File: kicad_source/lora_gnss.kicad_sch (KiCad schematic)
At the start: 32 parts, among them Q1 NTR4171P, SW3 SW_SPDT, U2 Ai-Thinker-Ra-01, U3 NEO-M8N, U5 24LC32, U6 BME280, U7 TPS3839DBZ, U8 TPS73630DBV, U9 MCP73832-2-OT

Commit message: glued project together
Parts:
- removed BT1: Battery_Cell, generationmake:KEYSTONE_1043, symbol Device:Battery_Cell
- removed C21, C22, C23: 2.2 uF, Capacitor_SMD:C_0603_1608Metric, symbol Device:C_Small
- removed D3: LED_Small, LED_SMD:LED_0603_1608Metric, symbol Device:LED_Small
- removed D4: MBR120, Diode_SMD:D_SOD-123, symbol Device:D_Schottky_Small
- removed F1: SF-1206S050, Fuse:Fuse_1206_3216Metric, symbol Device:Fuse
- removed Q1: NTR4171P, Package_TO_SOT_SMD:SOT-23, symbol Device:Q_PMOS_GSD
- removed R14, R16: 4k7, Resistor_SMD:R_0603_1608Metric, symbol Device:R_Small
- removed R15: 2k, Resistor_SMD:R_0603_1608Metric, symbol Device:R_Small
- removed SW3: SW_SPDT, Button_Switch_THT:SW_Slide-03_Wuerth-WS-SLTV_10x2.5x6.4_P2.54mm, symbol Switch:SW_SPDT_312
- removed U7: TPS3839DBZ, Package_TO_SOT_SMD:SOT-23, symbol Power_Supervisor:TPS3839DBZ
- removed U8: TPS73630DBV, Package_TO_SOT_SMD:SOT-23-5, symbol Regulator_Linear:TPS73630DBV
- removed U9: MCP73832-2-OT, Package_TO_SOT_SMD:SOT-23-5, symbol Battery_Management:MCP73832-2-OT
- added J1: BM04B-SRSS-TB, Connector_JST:JST_SH_BM04B-SRSS-TB_1x04-1MP_P1.00mm_Vertical, symbol Connector_Generic_MountingPin:Conn_01x04_MountingPin
- added R12, R4: 10k, Resistor_SMD:R_0603_1608Metric, symbol Device:R_Small
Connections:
- net +3V3: now also J1.2 (Pin_2), R12.1, R4.1
- net GND: now also J1.1 (Pin_1)
- net I2C_SCL: now also J1.4 (Pin_4), R12.2
- net I2C_SDA: now also J1.3 (Pin_3), R4.2
- no-connect marks 14 -> 12
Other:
- note added: "quiic connector"
- note removed: "charging current set to 500 mA (R15 = 2k)"
- title: RP2040LoRaTracker -> LoRaZeroHAT

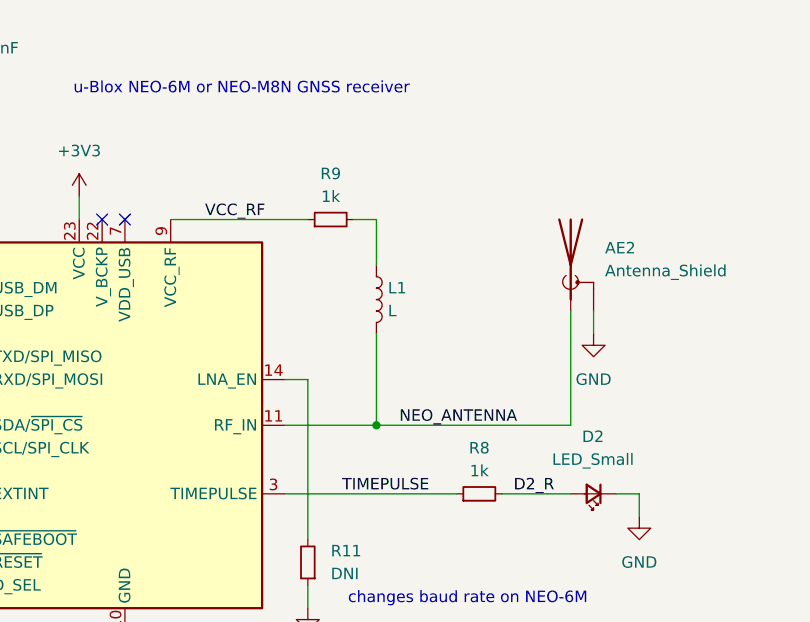
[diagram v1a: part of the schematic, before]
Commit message: connected schematic to layout
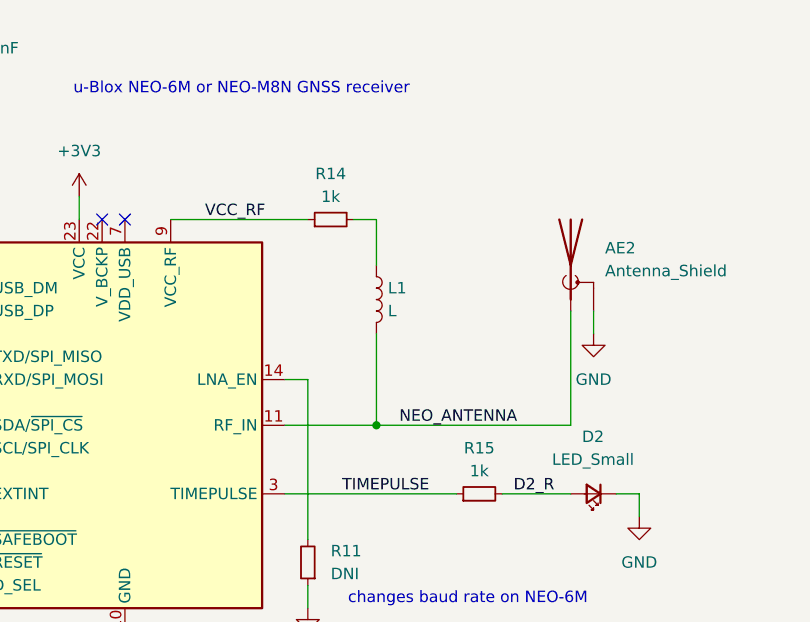
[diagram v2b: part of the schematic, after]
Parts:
- renumbered R9 to R14, R8 to R15
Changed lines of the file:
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@@
 		(dnp no)
 		(fields_autoplaced yes)
-		(property "Reference" "R8"
+		(property "Reference" "R15"
 			(at 127 76.2 90)
 			(effects
@@
 			(project "RP2040LoRaTracker"
 				(path "/143f7a5b-9016-4d2c-b741-f535648590f8/eaeb2dbb-82d1-4bb1-aa6e-4edb004b54b5"
-					(reference "R8")
+					(reference "R15")
 					(unit 1)
 				)
@@
 		(dnp no)
 		(fields_autoplaced yes)
-		(property "Reference" "R9"
+		(property "Reference" "R14"
 			(at 110.49 45.72 90)
 			(effects
@@
 			(project "RP2040LoRaTracker"
 				(path "/143f7a5b-9016-4d2c-b741-f535648590f8/eaeb2dbb-82d1-4bb1-aa6e-4edb004b54b5"
-					(reference "R9")
-					(unit 1)
-				)
+					(reference "R14")
+					(unit 1)
+				)

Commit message: made first connections
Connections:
- net +3V3 renamed +3.3V

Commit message: updated layout
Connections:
- net LORA_DIO0 renamed LORA_INT
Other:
- note added: "DIO0 is configured as interrupt"
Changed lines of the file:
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@@
+		)
+	)
+	(text "DIO0 is configured as interrupt"
+		(exclude_from_sim no)
+		(at 251.714 76.2 0)
+		(effects
+			(font
+				(size 1.27 1.27)
+			)
 		)
 	)
@@
 		)
 	)
-	(label "LORA_DIO0"
+	(label "LORA_INT"
 		(at 220.98 71.12 0)
 		(effects
@@
 		)
 	)
-	(global_label "LORA_DIO0"
+	(global_label "LORA_INT"
 		(shape output)
 		(at 234.95 71.12 0)
@@
 		)
 		(property "Intersheetrefs" "${INTERSHEET_REFS}"
-			(at 248.0348 71.12 0)
+			(at 246.5229 71.12 0)
 			(effects
 				(font

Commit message: schaltplan neu annotiert
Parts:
- renumbered AE2 to AE1, AE1 to AE2, C16 to C1, C17 to C2, C20 to C3, C18 to C4, C19 to C5, D2 to D1, L1 to L4, R10 to R12, R11 to R13, R4 to R15, R15 to R16, R12 to R17, U5 to U1, U3 to U2, U2 to U3, U6 to U4

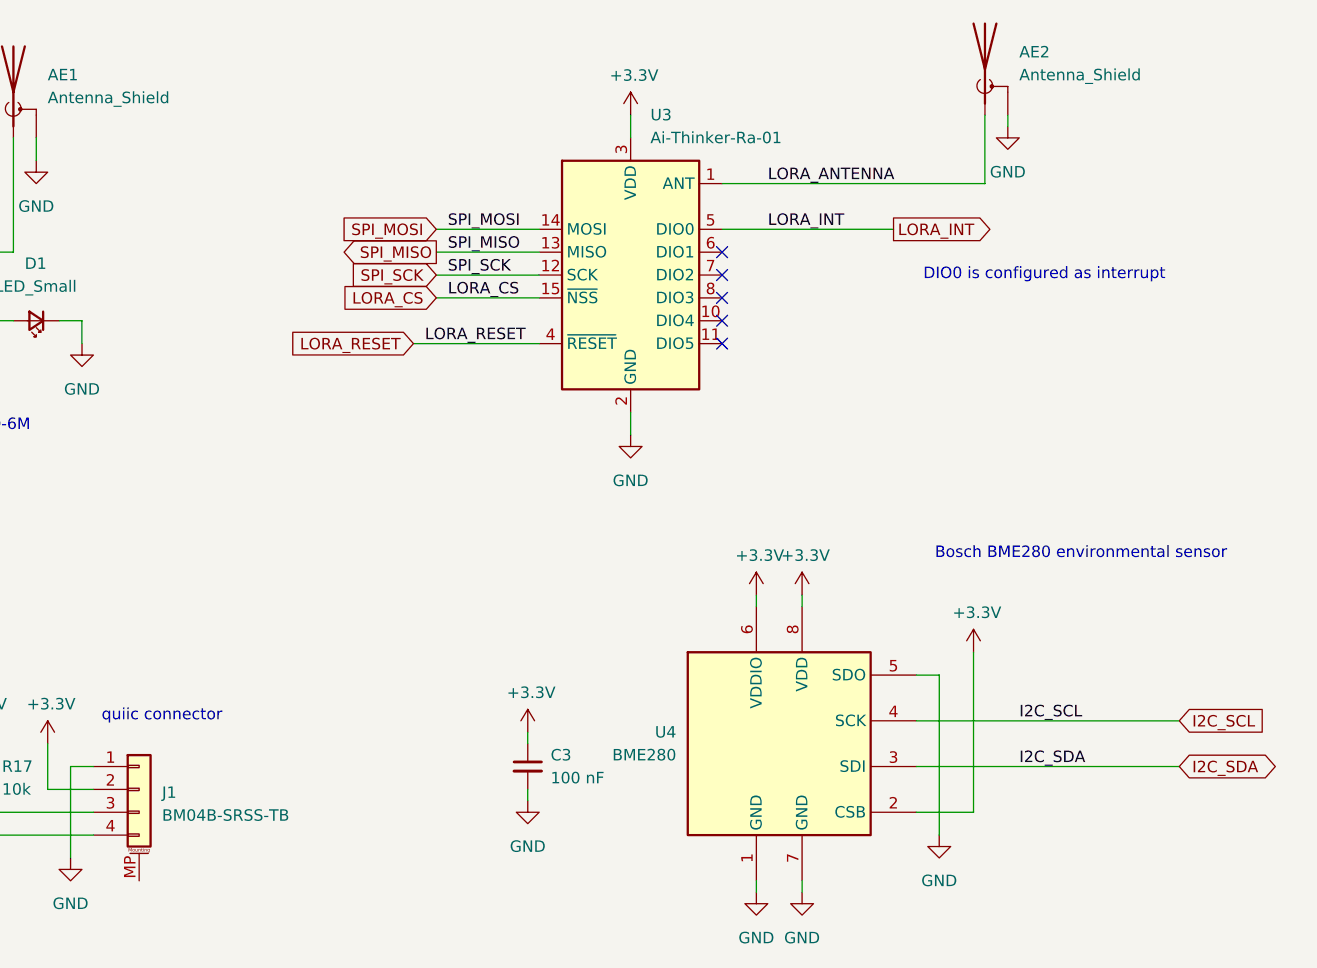
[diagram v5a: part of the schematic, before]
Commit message: updated layout
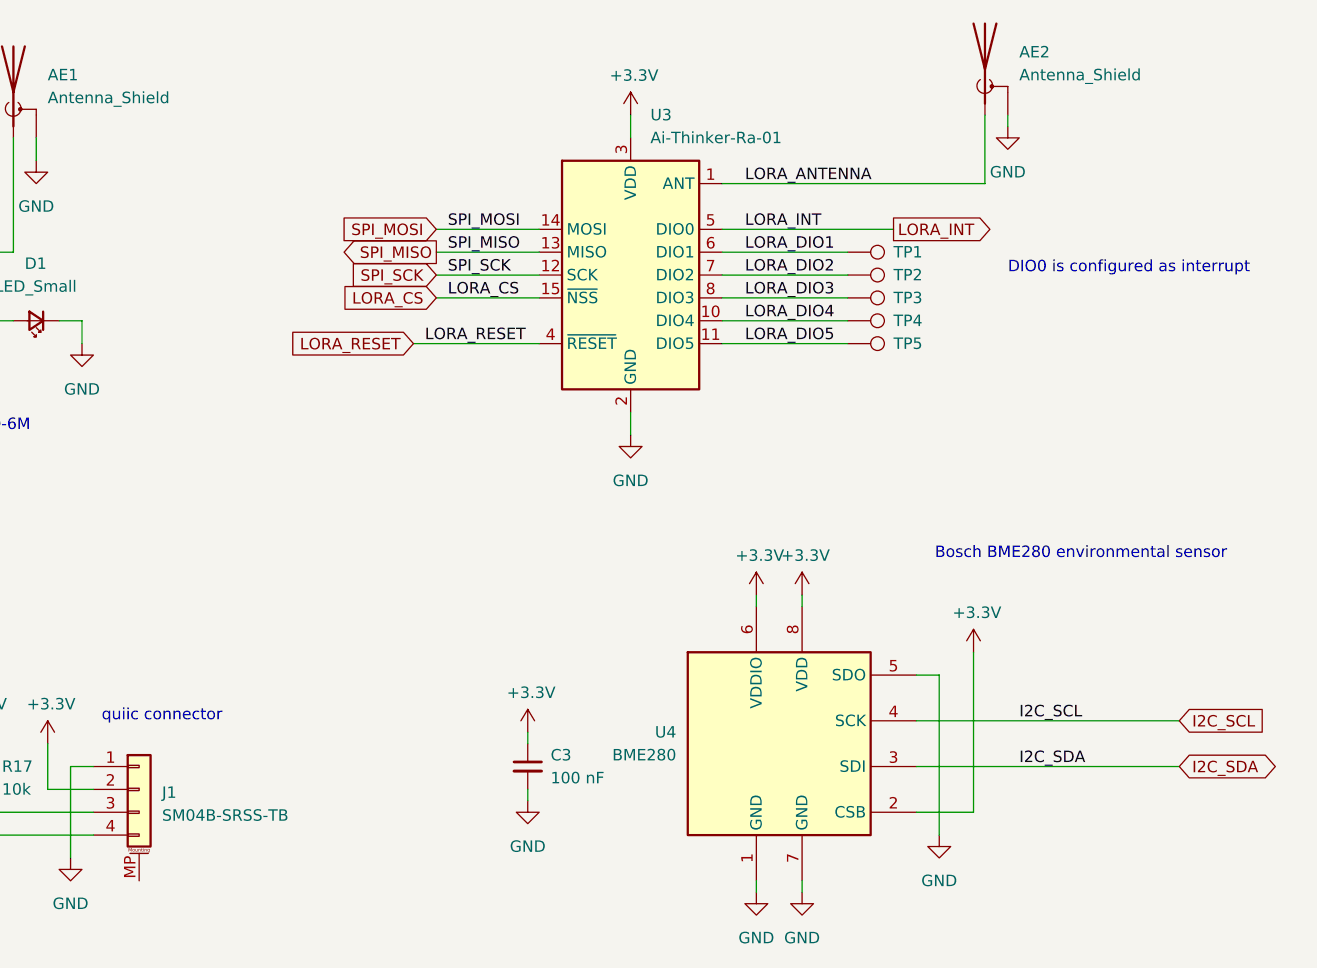
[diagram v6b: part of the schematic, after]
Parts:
- added TP1, TP2, TP3, TP4, TP5: TestPoint, TestPoint:TestPoint_Pad_D1.0mm, symbol Connector:TestPoint
- J1: value BM04B-SRSS-TB -> SM04B-SRSS-TB; footprint Connector_JST:JST_SH_BM04B-SRSS-TB_1x04-1MP_P1.00mm_Vertical -> Connector_JST:JST_SH_SM04B-SRSS-TB_1x04-1MP_P1.00mm_Horizontal
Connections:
- net LORA_DIO4: now reaches U3.10 (DIO4)
- net LORA_DIO4: now also TP4.1
- net LORA_DIO5: now reaches U3.11 (DIO5)
- net LORA_DIO5: now also TP5.1
- net LORA_DIO1: now reaches U3.6 (DIO1)
- net LORA_DIO1: now also TP1.1
- net LORA_DIO2: now reaches U3.7 (DIO2)
- net LORA_DIO2: now also TP2.1
- net LORA_DIO3: now reaches U3.8 (DIO3)
- net LORA_DIO3: now also TP3.1
- no-connect marks 12 -> 7

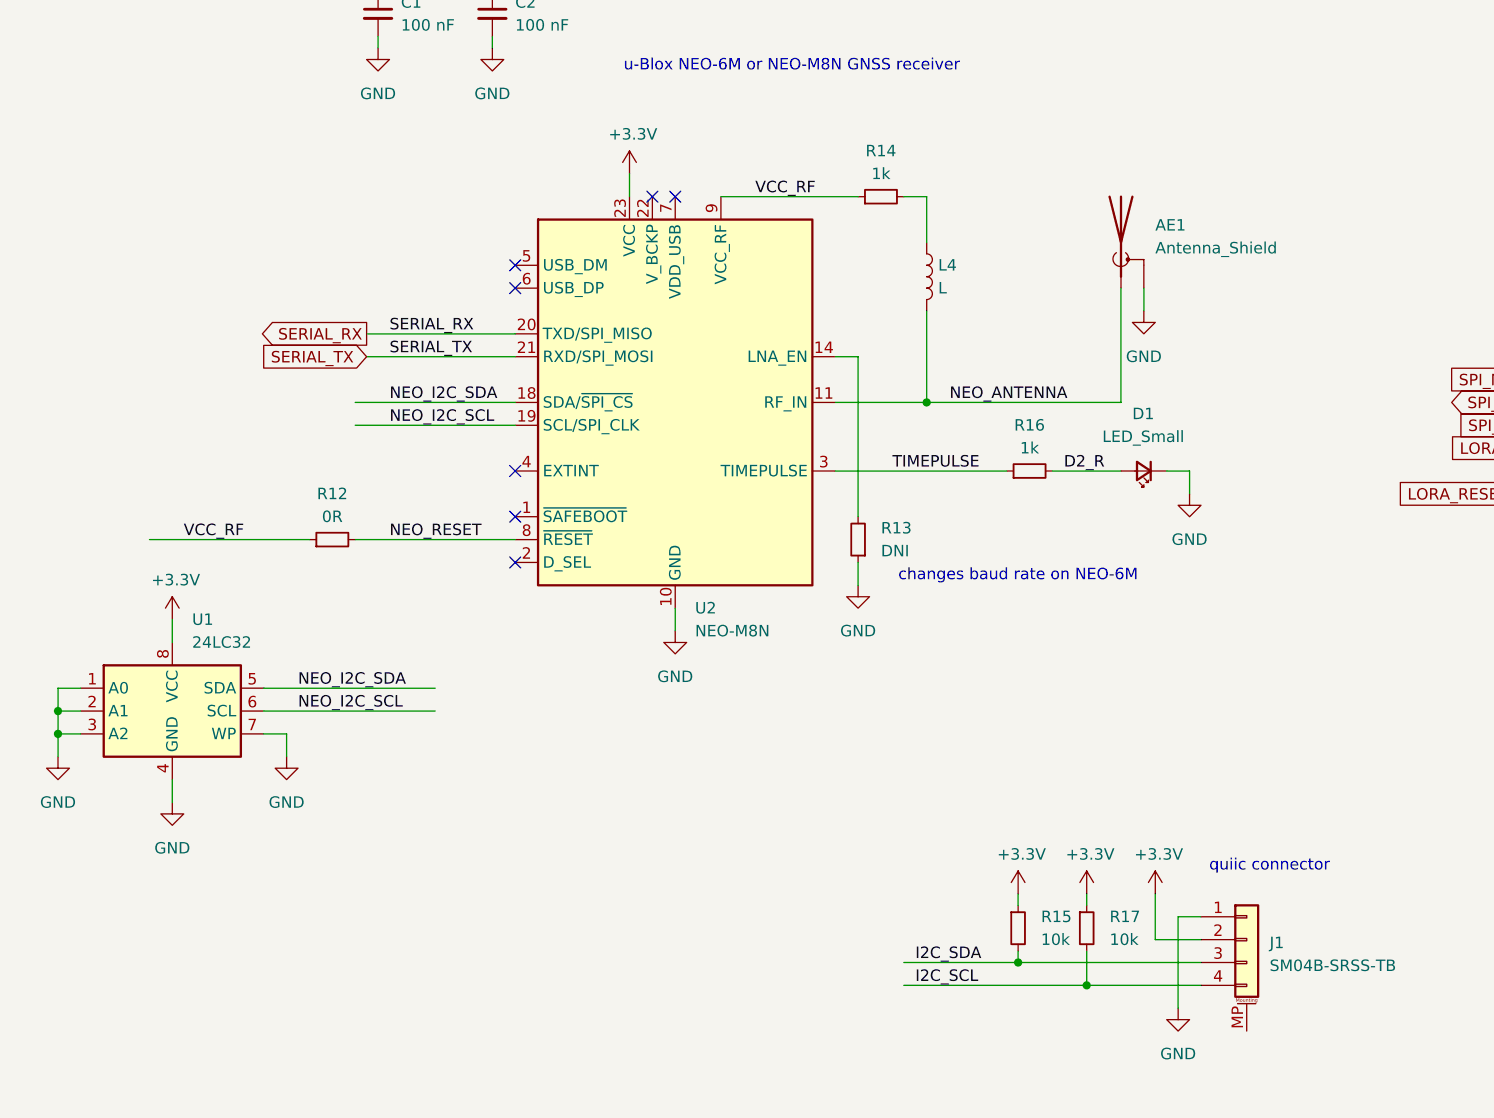
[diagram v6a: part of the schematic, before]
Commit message: added capacitor C6 on u-blox VCC_RF
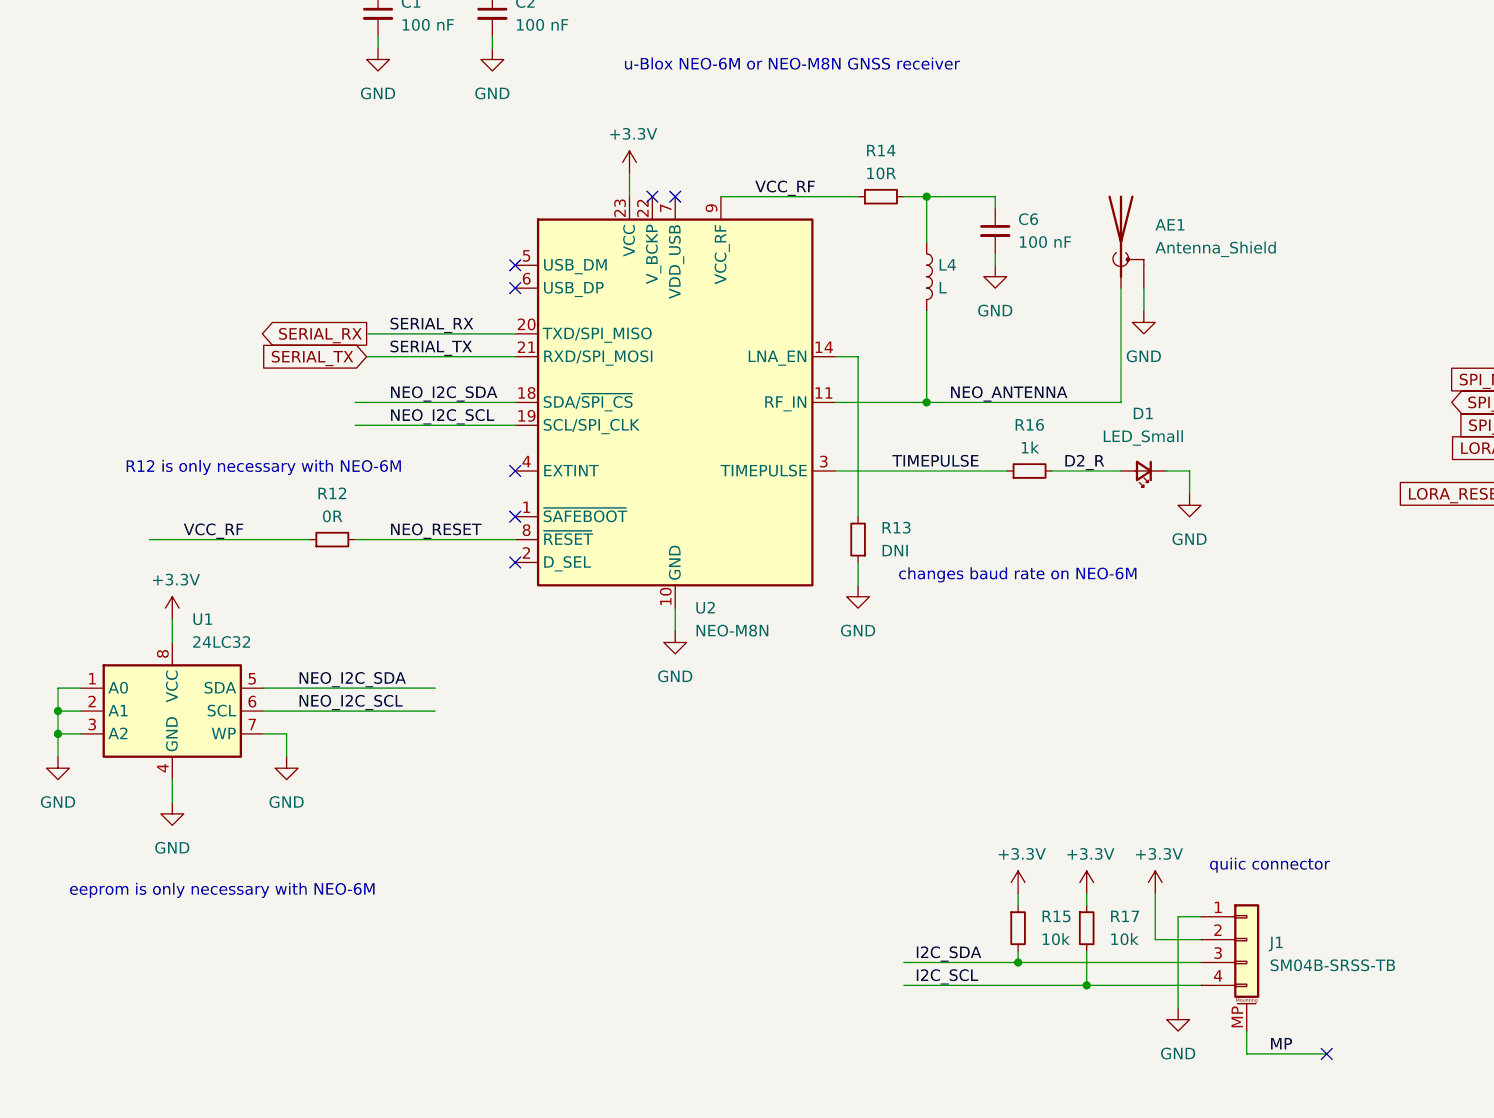
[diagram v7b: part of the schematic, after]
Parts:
- added C6: 100 nF, Capacitor_SMD:C_0603_1608Metric, symbol Device:C_Small
- R14: value 1k -> 10R
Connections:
- net GND: now also C6.2
- net at L4.1, R14.2: now also C6.1
- net MP: now reaches J1.MP (MountPin)
- no-connect marks 7 -> 8
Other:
- note added: "R12 is only necessary with NEO-6M"
- note added: "eeprom is only necessary with NEO-6M"
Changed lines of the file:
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@@
 	)
 	(junction
+		(at 115.57 50.8)
+		(diameter 0)
+		(color 0 0 0 0)
+	)
+	(junction
 		(at 125.73 135.89)
 		(diameter 0)
@@
 	)
 	(no_connect
+		(at 160.02 146.05)
+	)
+	(no_connect
 		(at 69.85 81.28)
 	)
@@
 	(wire
 		(pts
+			(xy 151.13 146.05) (xy 151.13 143.51)
+		)
+		(stroke
+			(width 0)
+			(type default)
+		)
+	)
+	(wire
+		(pts
+			(xy 115.57 50.8) (xy 123.19 50.8)
+		)
+		(stroke
+			(width 0)
+			(type default)
+		)
+	)
+	(wire
+		(pts
 			(xy 54.61 26.67) (xy 54.61 27.94)
 		)
@@
 	(wire
 		(pts
+			(xy 160.02 146.05) (xy 151.13 146.05)
+		)
+		(stroke
+			(width 0)
+			(type default)
+		)
+	)
+	(wire
+		(pts
 			(xy 219.71 111.76) (xy 219.71 113.03)
 		)
@@
 	(wire
 		(pts
+			(xy 123.19 50.8) (xy 123.19 52.07)
+		)
+		(stroke
+			(width 0)
+			(type default)
+		)
+	)
+	(wire
+		(pts
 			(xy 125.73 135.89) (xy 146.05 135.89)
 		)
@@
 	(wire
 		(pts
+			(xy 123.19 57.15) (xy 123.19 58.42)
+		)
+		(stroke
+			(width 0)
+			(type default)
+		)
+	)
+	(wire
+		(pts
 			(xy 195.58 31.75) (xy 195.58 33.02)
 		)
@@
 		)
 	)
+	(text "R12 is only necessary with NEO-6M"
+		(exclude_from_sim no)
+		(at 41.91 81.026 0)
+		(effects
+			(font
+				(size 1.27 1.27)
+			)
+		)
+	)
+	(text "eeprom is only necessary with NEO-6M"
+		(exclude_from_sim no)
+		(at 37.338 128.016 0)
+		(effects
+			(font
+				(size 1.27 1.27)
+			)
+		)
+	)
 	(text "changes baud rate on NEO-6M"
 		(exclude_from_sim no)
@@
 		)
 	)
+	(label "MP"
+		(at 153.67 146.05 0)
+		(effects
+			(font
+				(size 1.27 1.27)
+			)
+			(justify left bottom)
+		)
+	)
 	(label "TIMEPULSE"
 		(at 111.76 81.28 0)
@@
 	)
 	(symbol
+		(lib_id "power:GND")
+		(at 123.19 58.42 0)
+		(unit 1)
+		(exclude_from_sim no)
+		(in_bom yes)
+		(on_board yes)
+		(dnp no)
+		(fields_autoplaced yes)
+		(property "Reference" "#PWR40"
+			(at 123.19 64.77 0)
+			(effects
+				(font
+					(size 1.27 1.27)
+				)
+				(hide yes)
+			)
+		)
+		(property "Value" "GND"
+			(at 123.19 63.5 0)
+			(effects
+				(font
+					(size 1.27 1.27)
+				)
+			)
+		)
+		(property "Footprint" ""
+			(at 123.19 58.42 0)
+			(effects
+				(font
+					(size 1.27 1.27)
+				)
+				(hide yes)
+			)
+		)
+		(property "Datasheet" ""
+			(at 123.19 58.42 0)
+			(effects
+				(font
+					(size 1.27 1.27)
+				)
+				(hide yes)
+			)
+		)
+		(property "Description" "Power symbol creates a global label with name \"GND\" , ground"
+			(at 123.19 58.42 0)
+			(effects
+				(font
+					(size 1.27 1.27)
+				)
+				(hide yes)
+			)
+		)
+		(pin "1"
+		)
+		(instances
+			(project "LoRaZeroHAT"
+				(path "/143f7a5b-9016-4d2c-b741-f535648590f8/eaeb2dbb-82d1-4bb1-aa6e-4edb004b54b5"
+					(reference "#PWR40")
+					(unit 1)
+				)
+			)
+		)
+	)
+	(symbol
 		(lib_id "Device:R_Small")
 		(at 107.95 88.9 180)
@@
 			)
 		)
-		(property "Value" "1k"
+		(property "Value" "10R"
 			(at 110.49 48.26 90)
 			(effects
@@
 					(unit 1)
 				)
+			)
+		)
+	)
+	(symbol
+		(lib_id "Device:C_Small")
+		(at 123.19 54.61 0)
+		(unit 1)
+		(exclude_from_sim no)
+		(in_bom yes)
+		(on_board yes)
+		(dnp no)
+		(fields_autoplaced yes)
+		(property "Reference" "C6"
+			(at 125.73 53.3462 0)
+			(effects
+				(font
+					(size 1.27 1.27)
+				)
+				(justify left)
+			)
+		)
+		(property "Value" "100 nF"
+			(at 125.73 55.8862 0)
+			(effects
+				(font
+					(size 1.27 1.27)
+				)
+				(justify left)
+			)
+		)
+		(property "Footprint" "Capacitor_SMD:C_0603_1608Metric"
+			(at 123.19 54.61 0)
+			(effects
+				(font
+					(size 1.27 1.27)
+				)
+				(hide yes)
+			)
+		)
+		(property "Datasheet" "~"
+			(at 123.19 54.61 0)
+			(effects
+				(font
+					(size 1.27 1.27)
+				)
+				(hide yes)
+			)
+		)
+		(property "Description" "Unpolarized capacitor, small symbol"
+			(at 123.19 54.61 0)
+			(effects
+				(font
+					(size 1.27 1.27)
+				)
+				(hide yes)
+			)
+		)
+		(pin "2"
+		)
+		(pin "1"
+		)
+		(instances
+			(project "LoRaZeroHAT"
+				(path "/143f7a5b-9016-4d2c-b741-f535648590f8/eaeb2dbb-82d1-4bb1-aa6e-4edb004b54b5"
+					(reference "C6")
+					(unit 1)
+				)
